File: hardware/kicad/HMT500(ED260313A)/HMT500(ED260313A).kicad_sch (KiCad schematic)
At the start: 0 parts

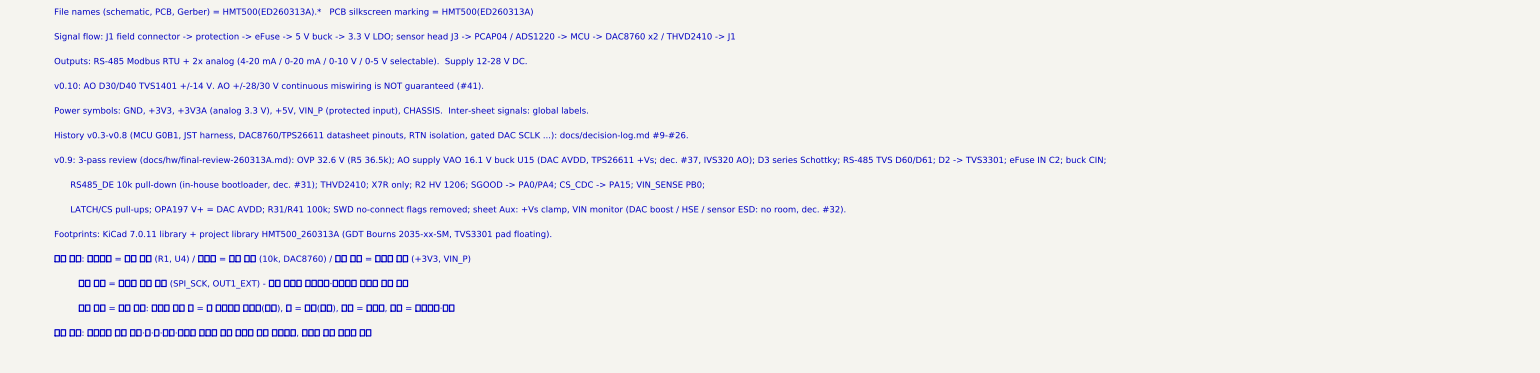
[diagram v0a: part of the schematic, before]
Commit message: Revise protection resistors for stocked JLC BOM R2
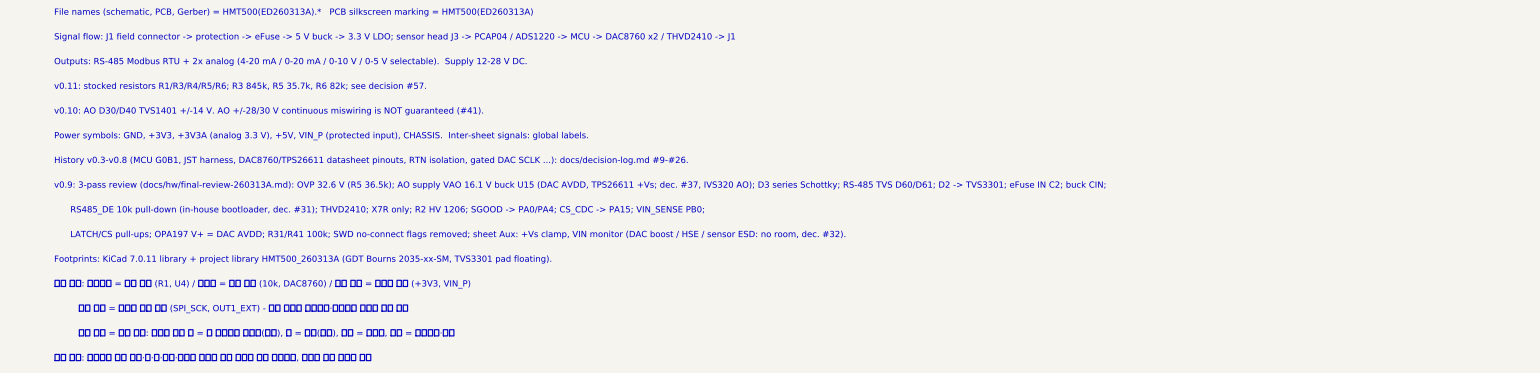
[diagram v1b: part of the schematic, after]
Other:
- note added: "v0.11: stocked resistors R1/R3/R4/R5/R6; R3 845k, R5 35.7k, R6 82k; see decision #57."
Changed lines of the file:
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@@
 (kicad_sch (version 20230121) (generator eeschema) (paper "A3")
-(title_block (title "HMT500(ED260313A)  Top") (date "2026-10-01") (rev "0.10") (company "DOTECH Co., Ltd.") (comment 1 "Project No. HMT500(ED260313A)  -  HMT500(ED260313A) oil moisture transmitter") (comment 2 "Design notes: docs/hw/circuit-design.md") (comment 3 "Pinouts checked vs manufacturer datasheets 2026-09-30 (STM32: KiCad lib)"))
+(title_block (title "HMT500(ED260313A)  Top") (date "2026-10-03") (rev "0.11") (company "DOTECH Co., Ltd.") (comment 1 "Project No. HMT500(ED260313A)  -  HMT500(ED260313A) oil moisture transmitter") (comment 2 "Design notes: docs/hw/circuit-design.md") (comment 3 "Pinouts checked vs manufacturer datasheets 2026-09-30 (STM32: KiCad lib)"))
 (sheet (at 20.32 35.56) (size 86.36 40.64) (fields_autoplaced) (stroke (width 0.1524) (type solid)) (fill (color 0 0 0 0.0000)) (property "Sheetname" "1. Connector & input protection" (at 20.32 34.798 0) (effects (font (size 1.8 1.8) bold) (justify left bottom))) (property "Sheetfile" "HMT500(ED260313A)_connector.kicad_sch" (at 20.32 76.962 0) (effects (font (size 1.27 1.27)) (justify left top))) (instances (project "HMT500(ED260313A)" (path "/1ebb025b-11bd-5f7c-aaab-41e2a750e8b3" (page "2")))))
 (text "Field connector, 2-stage bidirectional" (at 22.86 50.8 0) (effects (font (size 1.4 1.4)) (justify left bottom)))
@@
 (text "Signal flow: J1 field connector -> protection -> eFuse -> 5 V buck -> 3.3 V LDO; sensor head J3 -> PCAP04 / ADS1220 -> MCU -> DAC8760 x2 / THVD2410 -> J1" (at 30.48 161.036 0) (effects (font (size 1.4 1.4)) (justify left bottom)))
 (text "Outputs: RS-485 Modbus RTU + 2x analog (4-20 mA / 0-20 mA / 0-10 V / 0-5 V selectable).  Supply 12-28 V DC." (at 30.48 166.624 0) (effects (font (size 1.4 1.4)) (justify left bottom)))
-(text "v0.10: AO D30/D40 TVS1401 +/-14 V. AO +/-28/30 V continuous miswiring is NOT guaranteed (#41)." (at 30.48 172.212 0) (effects (font (size 1.4 1.4)) (justify left bottom)))
-(text "Power symbols: GND, +3V3, +3V3A (analog 3.3 V), +5V, VIN_P (protected input), CHASSIS.  Inter-sheet signals: global labels." (at 30.48 177.8 0) (effects (font (size 1.4 1.4)) (justify left bottom)))
-(text "History v0.3-v0.8 (MCU G0B1, JST harness, DAC8760/TPS26611 datasheet pinouts, RTN isolation, gated DAC SCLK ...): docs/decision-log.md #9-#26." (at 30.48 183.388 0) (effects (font (size 1.4 1.4)) (justify left bottom)))
-(text "v0.9: 3-pass review (docs/hw/final-review-260313A.md): OVP 32.6 V (R5 36.5k); AO supply VAO 16.1 V buck U15 (DAC AVDD, TPS26611 +Vs; dec. #37, IVS320 AO); D3 series Schottky; RS-485 TVS D60/D61; D2 -> TVS3301; eFuse IN C2; buck CIN;" (at 30.48 188.976 0) (effects (font (size 1.4 1.4)) (justify left bottom)))
-(text "      RS485_DE 10k pull-down (in-house bootloader, dec. #31); THVD2410; X7R only; R2 HV 1206; SGOOD -> PA0/PA4; CS_CDC -> PA15; VIN_SENSE PB0;" (at 30.48 194.564 0) (effects (font (size 1.4 1.4)) (justify left bottom)))
-(text "      LATCH/CS pull-ups; OPA197 V+ = DAC AVDD; R31/R41 100k; SWD no-connect flags removed; sheet Aux: +Vs clamp, VIN monitor (DAC boost / HSE / sensor ESD: no room, dec. #32)." (at 30.48 200.152 0) (effects (font (size 1.4 1.4)) (justify left bottom)))
-(text "Footprints: KiCad 7.0.11 library + project library HMT500_260313A (GDT Bourns 2035-xx-SM, TVS3301 pad floating)." (at 30.48 205.74 0) (effects (font (size 1.4 1.4)) (justify left bottom)))
-(text "표기 규칙: 부품번호 = 굵은 글자 (R1, U4) / 부품값 = 보통 글자 (10k, DAC8760) / 전원 네트 = 기울인 글자 (+3V3, VIN_P)" (at 30.48 211.328 0) (effects (font (face "NanumGothic") (size 1.4 1.4)) (justify left bottom)))
-(text "         신호 네트 = 테두리 있는 라벨 (SPI_SCK, OUT1_EXT) - 네트 이름은 부품번호·부품명과 겹치지 않게 지음" (at 30.48 216.916 0) (effects (font (face "NanumGothic") (size 1.4 1.4)) (justify left bottom)))
-(text "         라벨 모양 = 신호 방향: 뾰족한 쪽이 밖 = 이 시트에서 내보냄(출력), 안 = 받음(입력), 양쪽 = 양방향, 네모 = 아날로그·수동" (at 30.48 222.504 0) (effects (font (face "NanumGothic") (size 1.4 1.4)) (justify left bottom)))
-(text "글자 겹침: 생성기가 부품 몸체·핀·선·라벨·메모와 겹치지 않는 자리에 자동 배치하고, 겹치면 생성 실패로 처리" (at 30.48 228.092 0) (effects (font (face "NanumGothic") (size 1.4 1.4)) (justify left bottom)))
+(text "v0.11: stocked resistors R1/R3/R4/R5/R6; R3 845k, R5 35.7k, R6 82k; see decision #57." (at 30.48 172.212 0) (effects (font (size 1.4 1.4)) (justify left bottom)))
+(text "v0.10: AO D30/D40 TVS1401 +/-14 V. AO +/-28/30 V continuous miswiring is NOT guaranteed (#41)." (at 30.48 177.8 0) (effects (font (size 1.4 1.4)) (justify left bottom)))
+(text "Power symbols: GND, +3V3, +3V3A (analog 3.3 V), +5V, VIN_P (protected input), CHASSIS.  Inter-sheet signals: global labels." (at 30.48 183.388 0) (effects (font (size 1.4 1.4)) (justify left bottom)))
+(text "History v0.3-v0.8 (MCU G0B1, JST harness, DAC8760/TPS26611 datasheet pinouts, RTN isolation, gated DAC SCLK ...): docs/decision-log.md #9-#26." (at 30.48 188.976 0) (effects (font (size 1.4 1.4)) (justify left bottom)))
+(text "v0.9: 3-pass review (docs/hw/final-review-260313A.md): OVP 32.6 V (R5 36.5k); AO supply VAO 16.1 V buck U15 (DAC AVDD, TPS26611 +Vs; dec. #37, IVS320 AO); D3 series Schottky; RS-485 TVS D60/D61; D2 -> TVS3301; eFuse IN C2; buck CIN;" (at 30.48 194.564 0) (effects (font (size 1.4 1.4)) (justify left bottom)))
+(text "      RS485_DE 10k pull-down (in-house bootloader, dec. #31); THVD2410; X7R only; R2 HV 1206; SGOOD -> PA0/PA4; CS_CDC -> PA15; VIN_SENSE PB0;" (at 30.48 200.152 0) (effects (font (size 1.4 1.4)) (justify left bottom)))
+(text "      LATCH/CS pull-ups; OPA197 V+ = DAC AVDD; R31/R41 100k; SWD no-connect flags removed; sheet Aux: +Vs clamp, VIN monitor (DAC boost / HSE / sensor ESD: no room, dec. #32)." (at 30.48 205.74 0) (effects (font (size 1.4 1.4)) (justify left bottom)))
+(text "Footprints: KiCad 7.0.11 library + project library HMT500_260313A (GDT Bourns 2035-xx-SM, TVS3301 pad floating)." (at 30.48 211.328 0) (effects (font (size 1.4 1.4)) (justify left bottom)))
+(text "표기 규칙: 부품번호 = 굵은 글자 (R1, U4) / 부품값 = 보통 글자 (10k, DAC8760) / 전원 네트 = 기울인 글자 (+3V3, VIN_P)" (at 30.48 216.916 0) (effects (font (face "NanumGothic") (size 1.4 1.4)) (justify left bottom)))
+(text "         신호 네트 = 테두리 있는 라벨 (SPI_SCK, OUT1_EXT) - 네트 이름은 부품번호·부품명과 겹치지 않게 지음" (at 30.48 222.504 0) (effects (font (face "NanumGothic") (size 1.4 1.4)) (justify left bottom)))
+(text "         라벨 모양 = 신호 방향: 뾰족한 쪽이 밖 = 이 시트에서 내보냄(출력), 안 = 받음(입력), 양쪽 = 양방향, 네모 = 아날로그·수동" (at 30.48 228.092 0) (effects (font (face "NanumGothic") (size 1.4 1.4)) (justify left bottom)))
+(text "글자 겹침: 생성기가 부품 몸체·핀·선·라벨·메모와 겹치지 않는 자리에 자동 배치하고, 겹치면 생성 실패로 처리" (at 30.48 233.68 0) (effects (font (face "NanumGothic") (size 1.4 1.4)) (justify left bottom)))
 (sheet_instances (path "/" (page "1")))
 )
